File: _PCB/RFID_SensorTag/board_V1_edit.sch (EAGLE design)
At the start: 17 parts, among them M2 BATTERY-CHARGER-LI-PROT, U1 MAXIM_ELECTRONICS_MAX40200AUK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, X1 53048-02

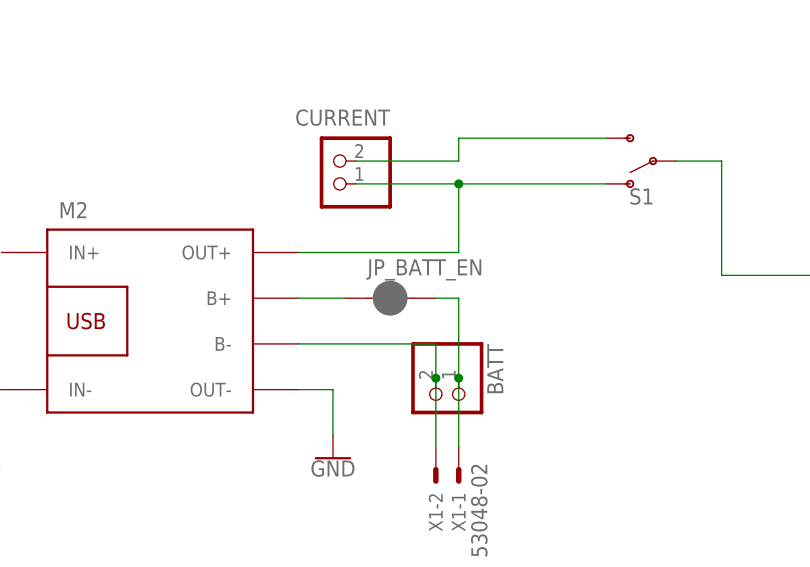
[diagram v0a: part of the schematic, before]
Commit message: RFID system PCB V1 edit
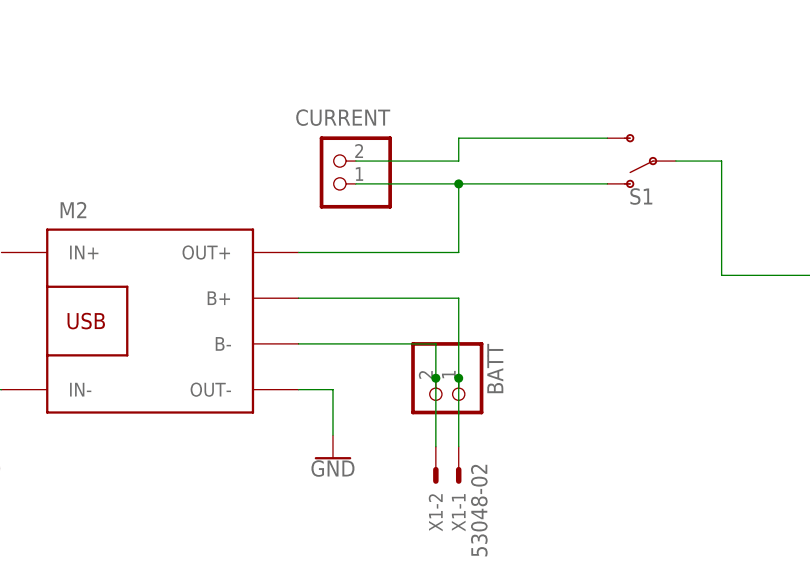
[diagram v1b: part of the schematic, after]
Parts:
- removed JP_BATT_EN: JUMPER-SMT_2_NC_PASTE_SILK, SparkFun-Jumpers:JUMPER-SMT_2_NC_PASTE_SILK
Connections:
- removed net N$3: BATT.1, JP_BATT_EN.2, X1-1.S
- removed net N$6: JP_BATT_EN.1, M2.B+
- new net N$1: BATT.1, M2.B+, X1-1.S
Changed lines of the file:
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@@
 <setting verticaltext="up"/>
 </settings>
-<grid distance="0.1" unitdist="inch" unit="inch" style="lines" multiple="1" display="no" altdistance="0.01" altunitdist="inch" altunit="inch"/>
+<grid distance="0.05" unitdist="inch" unit="inch" style="lines" multiple="1" display="no" altdistance="0.01" altunitdist="inch" altunit="inch"/>
 <layers>
 <layer number="1" name="Top" color="4" fill="1" visible="no" active="no"/>
@@
 <part name="U1" library="Maxim Electronics - MAX40200AUK+" deviceset="MAXIM_ELECTRONICS_MAX40200AUK+" device="MAXIM_ELECTRONICS_MAX40200AUK+_0_0"/>
 <part name="BATT" library="pinhead" library_urn="urn:adsk.eagle:library:325" deviceset="PINHD-1X2" device="" package3d_urn="urn:adsk.eagle:package:22435/2"/>
-<part name="JP_BATT_EN" library="SparkFun-Jumpers" library_urn="urn:adsk.eagle:library:528" deviceset="JUMPER-SMT_2_NC_PASTE" device="_SILK" package3d_urn="urn:adsk.eagle:package:39282/1" value=""/>
 <part name="C4" library="rcl" library_urn="urn:adsk.eagle:library:334" deviceset="C-EU" device="C0805" package3d_urn="urn:adsk.eagle:package:23617/2" value="100nF"/>
 </parts>
@@
 <attribute name="NAME" x="71.755" y="34.29" size="1.778" layer="95" rot="R270"/>
 <attribute name="VALUE" x="60.96" y="34.29" size="1.778" layer="96" rot="R270"/>
-</instance>
-<instance part="JP_BATT_EN" gate="G$1" x="60.96" y="39.37" smashed="yes">
-<attribute name="NAME" x="58.42" y="41.91" size="1.778" layer="95" font="vector"/>
-<attribute name="VALUE" x="58.42" y="36.83" size="1.778" layer="96" font="vector" align="top-left"/>
 </instance>
 <instance part="C4" gate="G$1" x="151.13" y="38.1" smashed="yes">
@@
 </segment>
 </net>
-<net name="N$3" class="1">
-<segment>
-<pinref part="BATT" gate="G$1" pin="1"/>
-<pinref part="X1" gate="-1" pin="S"/>
-<wire x1="68.58" y1="30.48" x2="68.58" y2="22.86" width="0.1524" layer="91"/>
-<wire x1="68.58" y1="30.48" x2="68.58" y2="39.37" width="0.1524" layer="91"/>
-<junction x="68.58" y="30.48"/>
-<pinref part="JP_BATT_EN" gate="G$1" pin="2"/>
-<wire x1="66.04" y1="39.37" x2="68.58" y2="39.37" width="0.1524" layer="91"/>
-</segment>
-</net>
 <net name="N$5" class="1">
 <segment>
@@
 <wire x1="66.04" y1="34.29" x2="50.8" y2="34.29" width="0.1524" layer="91"/>
 <junction x="66.04" y="30.48"/>
-</segment>
-</net>
-<net name="N$6" class="1">
-<segment>
-<pinref part="M2" gate="G$1" pin="B+"/>
-<pinref part="JP_BATT_EN" gate="G$1" pin="1"/>
-<wire x1="50.8" y1="39.37" x2="55.88" y2="39.37" width="0.1524" layer="91"/>
 </segment>
 </net>
@@
 </segment>
 </net>
+<net name="N$1" class="1">
+<segment>
+<pinref part="X1" gate="-1" pin="S"/>
+<pinref part="BATT" gate="G$1" pin="1"/>
+<wire x1="68.58" y1="30.48" x2="68.58" y2="22.86" width="0.1524" layer="91"/>
+<pinref part="M2" gate="G$1" pin="B+"/>
+<wire x1="50.8" y1="39.37" x2="68.58" y2="39.37" width="0.1524" layer="91"/>
+<wire x1="68.58" y1="30.48" x2="68.58" y2="39.37" width="0.1524" layer="91"/>
+<junction x="68.58" y="30.48"/>
+</segment>
+</net>
